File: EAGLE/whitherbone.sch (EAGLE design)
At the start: 227 parts, among them IC10 TXS0108ERGYR, IC11 TXS0108ERGYR, IC12 TPS2051BDGN, IC13 SN74AUC1G74, IC14 TPD4S012DRY, IC15 TPD4S012DRY, IC17 SN74LVC2G241DCUR, IC18 TL1963ADCQR, IC19 AP2112K-1.8TRG1 3.3V, IC2 SN74LVC1G07DCK, IC4 7805T, IC7 IP4283CZ10-TBR, IC8 IP4283CZ10-TBR, IC9 TDA19988BHN/C1,557, J1 1-1747981-1, Q2 32.768kHz, Q4 24 MHz, T1 BSS138W-7-F, T3 BSS138W-7-F, T4 BSS138W-7-F, U1 OSD3358-512M-BSM, U2 A3967SLBTR, X2 SCHA5B0200, X4 10118192-0001LF

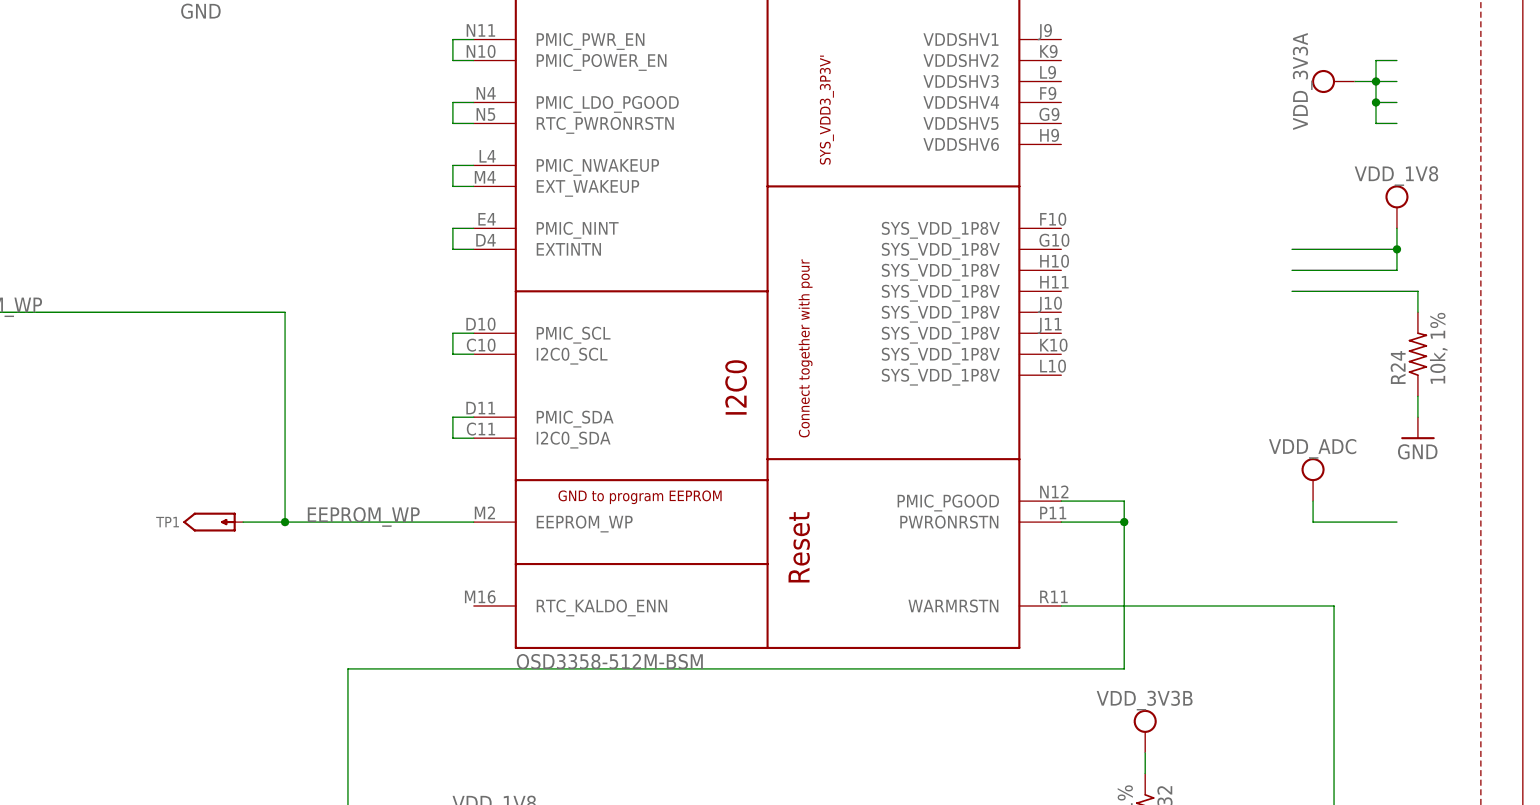
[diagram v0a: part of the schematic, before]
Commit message: Some minor power fixups
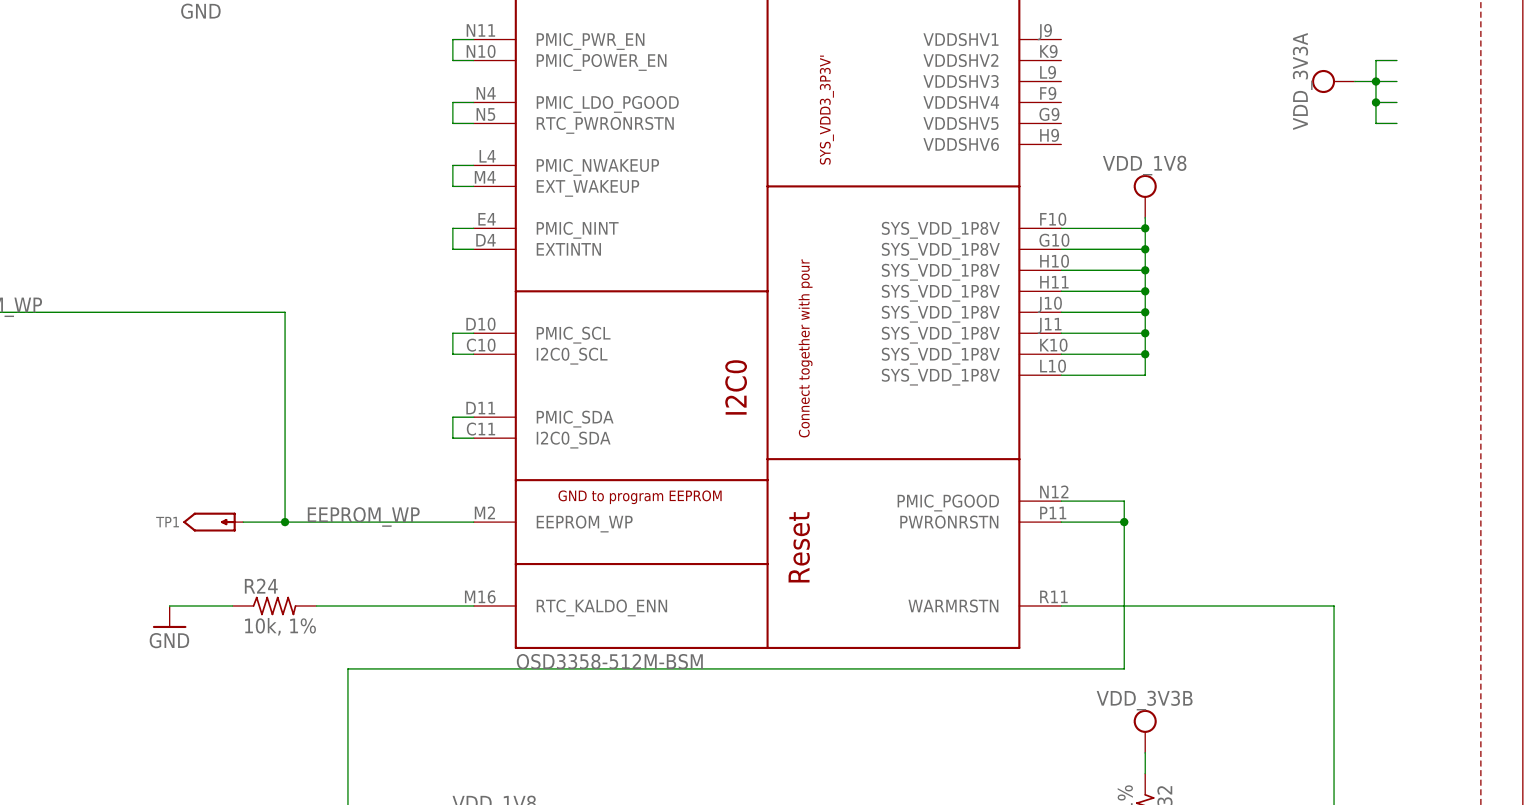
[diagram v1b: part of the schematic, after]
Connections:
- net N$22: now also U1A.RTC_KALDO_ENN
- net VDD_1V8: now also U1A.SYS_VDD_1P8V@1, U1A.SYS_VDD_1P8V@2, U1A.SYS_VDD_1P8V@3, U1A.SYS_VDD_1P8V@4, U1A.SYS_VDD_1P8V@5, U1A.SYS_VDD_1P8V@6, U1A.SYS_VDD_1P8V@7, U1A.SYS_VDD_1P8V@8
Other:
- moved on the sheet: R24
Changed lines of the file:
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@@
 <part name="SUPPLY7" library="GHI-PowerGoundSupply" deviceset="VDD_3V3A" device=""/>
 <part name="SUPPLY32" library="GHI-PowerGoundSupply" deviceset="VDD_5V" device=""/>
-<part name="SUPPLY4" library="GHI-PowerGoundSupply" deviceset="VDD_ADC" device=""/>
 <part name="SUPPLY11" library="GHI-PowerGoundSupply" deviceset="VDD_CORE" device=""/>
 <part name="SUPPLY5" library="GHI-PowerGoundSupply" deviceset="VDD_MPU" device=""/>
@@
 <instance part="SUPPLY14" gate="G$1" x="762" y="228.6"/>
 <instance part="SUPPLY6" gate="G$1" x="754.38" y="200.66" rot="R90"/>
-<instance part="SUPPLY12" gate="G$1" x="817.88" y="452.12"/>
+<instance part="SUPPLY12" gate="G$1" x="787.4" y="453.39"/>
 <instance part="SUPPLY7" gate="G$1" x="810.26" y="467.36" rot="R90"/>
 <instance part="SUPPLY32" gate="G$1" x="701.04" y="571.5"/>
-<instance part="SUPPLY4" gate="G$1" x="807.72" y="419.1"/>
 <instance part="SUPPLY11" gate="G$1" x="749.3" y="218.44"/>
 <instance part="SUPPLY5" gate="G$1" x="749.3" y="205.74" rot="R90"/>
@@
 <instance part="GND23" gate="1" x="673.1" y="477.52"/>
 <instance part="SUPPLY39" gate="G$1" x="789.94" y="548.64" rot="R270"/>
-<instance part="R24" gate="G$1" x="820.42" y="434.34" rot="R90"/>
-<instance part="GND10" gate="1" x="820.42" y="424.18"/>
+<instance part="R24" gate="G$1" x="681.99" y="403.86"/>
+<instance part="GND10" gate="1" x="669.29" y="401.32"/>
 <instance part="R8" gate="G$1" x="53.34" y="535.94" rot="R90"/>
 <instance part="R1" gate="G$1" x="459.74" y="154.94" rot="R90"/>
@@
 <pinref part="GND10" gate="1" pin="GND"/>
 <pinref part="R24" gate="G$1" pin="1"/>
-<wire x1="820.42" y1="426.72" x2="820.42" y2="429.26" width="0.1524" layer="91"/>
+<wire x1="669.29" y1="403.86" x2="676.91" y2="403.86" width="0.1524" layer="91"/>
 </segment>
 <segment>
@@
 <segment>
 <pinref part="SUPPLY12" gate="G$1" pin="VDD_1V8"/>
-<wire x1="817.88" y1="449.58" x2="817.88" y2="447.04" width="0.1524" layer="91"/>
-<wire x1="817.88" y1="447.04" x2="817.88" y2="444.5" width="0.1524" layer="91"/>
-<wire x1="817.88" y1="444.5" x2="805.18" y2="444.5" width="0.1524" layer="91"/>
-<wire x1="805.18" y1="447.04" x2="817.88" y2="447.04" width="0.1524" layer="91"/>
-<junction x="817.88" y="447.04"/>
+<wire x1="787.4" y1="450.85" x2="787.4" y2="449.58" width="0.1524" layer="91"/>
+<wire x1="787.4" y1="449.58" x2="787.4" y2="447.04" width="0.1524" layer="91"/>
+<wire x1="787.4" y1="447.04" x2="777.24" y2="447.04" width="0.1524" layer="91"/>
+<wire x1="777.24" y1="449.58" x2="787.4" y2="449.58" width="0.1524" layer="91"/>
+<junction x="787.4" y="449.58"/>
+<pinref part="U1" gate="A" pin="SYS_VDD_1P8V@3"/>
+<wire x1="777.24" y1="444.5" x2="787.4" y2="444.5" width="0.1524" layer="91"/>
+<wire x1="787.4" y1="444.5" x2="787.4" y2="447.04" width="0.1524" layer="91"/>
+<pinref part="U1" gate="A" pin="SYS_VDD_1P8V@4"/>
+<wire x1="777.24" y1="441.96" x2="787.4" y2="441.96" width="0.1524" layer="91"/>
+<wire x1="787.4" y1="441.96" x2="787.4" y2="444.5" width="0.1524" layer="91"/>
+<pinref part="U1" gate="A" pin="SYS_VDD_1P8V@5"/>
+<wire x1="777.24" y1="439.42" x2="787.4" y2="439.42" width="0.1524" layer="91"/>
+<wire x1="787.4" y1="439.42" x2="787.4" y2="441.96" width="0.1524" layer="91"/>
+<wire x1="777.24" y1="436.88" x2="787.4" y2="436.88" width="0.1524" layer="91"/>
+<wire x1="787.4" y1="436.88" x2="787.4" y2="439.42" width="0.1524" layer="91"/>
+<pinref part="U1" gate="A" pin="SYS_VDD_1P8V@7"/>
+<wire x1="777.24" y1="434.34" x2="787.4" y2="434.34" width="0.1524" layer="91"/>
+<wire x1="787.4" y1="434.34" x2="787.4" y2="436.88" width="0.1524" layer="91"/>
+<pinref part="U1" gate="A" pin="SYS_VDD_1P8V@8"/>
+<wire x1="777.24" y1="431.8" x2="787.4" y2="431.8" width="0.1524" layer="91"/>
+<wire x1="787.4" y1="431.8" x2="787.4" y2="434.34" width="0.1524" layer="91"/>
+<junction x="787.4" y="447.04"/>
+<junction x="787.4" y="444.5"/>
+<junction x="787.4" y="441.96"/>
+<junction x="787.4" y="439.42"/>
+<junction x="787.4" y="436.88"/>
+<junction x="787.4" y="434.34"/>
+<pinref part="U1" gate="A" pin="SYS_VDD_1P8V@1"/>
+<pinref part="U1" gate="A" pin="SYS_VDD_1P8V@2"/>
+<pinref part="U1" gate="A" pin="SYS_VDD_1P8V@6"/>
 </segment>
 <segment>
@@
 <net name="VDD_ADC" class="0">
 <segment>
-<pinref part="SUPPLY4" gate="G$1" pin="VDD_ADC"/>
-<wire x1="817.88" y1="414.02" x2="807.72" y2="414.02" width="0.1524" layer="91"/>
-<wire x1="807.72" y1="414.02" x2="807.72" y2="416.56" width="0.1524" layer="91"/>
-</segment>
-<segment>
 <pinref part="SUPPLY19" gate="G$1" pin="VDD_ADC"/>
 <wire x1="327.66" y1="546.1" x2="312.42" y2="546.1" width="0.1524" layer="91"/>
@@
 <net name="N$22" class="0">
 <segment>
-<wire x1="805.18" y1="441.96" x2="820.42" y2="441.96" width="0.1524" layer="91"/>
+<wire x1="706.12" y1="403.86" x2="687.07" y2="403.86" width="0.1524" layer="91"/>
 <pinref part="R24" gate="G$1" pin="2"/>
-<wire x1="820.42" y1="441.96" x2="820.42" y2="439.42" width="0.1524" layer="91"/>
+<pinref part="U1" gate="A" pin="RTC_KALDO_ENN"/>
 </segment>
 </net>

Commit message: Move WiFi signals to 1.8V and remove level shifters
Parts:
- removed C10: 1uF, rcl:C-USC0402K
- removed C19: 10uF, 6.3V, rcl:C-USC0603K
- removed C25, C45: .1uF, 6.3V, rcl:C-USC0402K
- removed D2: STPS140A DNP, GHI:DIODE_SMA
- removed D3, D4: STPS140A, GHI:DIODE_SMA
- removed D8: BAT54C, diode:BAT54C
- removed IC10, IC11: TXS0108ERGYR, GHI-IC:TXS0108ERGYR
- removed IC18: TL1963ADCQR, GHI-IC:TL1963A
- removed IC19: AP2112K-1.8TRG1 3.3V, GHI:5PIN_REG
- removed R10, R11: 150k, rcl:R-US_R0402
- removed R106: 1.5k, rcl:R-US_R0402
- removed R108, R109, R97: DNP 1k, rcl:R-US_R0402
- removed R126, R127, R128, R129, R130, R131, R134, R135, R136, R86: 33, 5%, rcl:R-US_R0603
- removed R89: 1k, rcl:R-US_R0402
- removed R91: 0 DNP, rcl:R-US_R0402
- removed R93: 7.15k, rcl:R-US_R0402
- removed R94: 4.12k, rcl:R-US_R0402
- removed R95: 1M, rcl:R-US_R0402
- removed TP23: PTR1B1,27, testpad:PTR1B1,27
- added FB7: 1k BLM15AG102SN1D, rcl:R-US_R0402
- FB1: value 220 Ohm 800mA -> 1k BLM15AG102SN1D; device GHI-BasicComponents:FB-(INCH)-0805 -> rcl:R-US_R0402
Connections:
- removed net 5V_IN: C19.1, D8.CC, FB1.P$2, IC18.IN, R95.1
- removed net ALT.BT.EN: IC11.B3, R135.2
- removed net ALT.BUFF.OE: IC10.OE, IC11.OE, R106.1, R131.1
- removed net ALT.WL.CLK: IC10.B5, R126.2
- removed net ALT.WL.CMD: IC10.B6, R86.2
- removed net ALT.WL.D0: IC10.B1, R130.2
- removed net ALT.WL.D1: IC10.B2, R129.2
- removed net ALT.WL.D2: IC10.B3, R128.2
- removed net ALT.WL.D3: IC10.B4, R127.2
- removed net ALT.WL.EN: IC11.B2, R136.2
- removed net ALT.WL.IRQ: IC11.B8, R134.2
- removed net BT_EN.SIP: R135.1, U1D.MII1_TXD0
- removed net BT_HCI_CTS.SIP: IC11.B5, R108.1, U1D.MDIO
- removed net BT_HCI_RTS.SIP: IC11.B7, R109.1, U1D.MDC
- removed net BT_HCI_RX.SIP: IC11.B6, U1D.MII1_RXD3
- removed net BT_HCI_TX.SIP: IC11.B1, U1D.MII1_RXD2
- removed net CLKOUT2: IC11.B4
- removed net LS_BUF_OE: R131.2, U1D.MII1_RX_CLK
- removed net N$30: R9.2
- removed net N$9: IC18.ADJ, R93.2, R94.1
- removed net SELECT_5V: D2.K, D3.K, D4.K, FB1.P$1, R97.1, TP23.TP
- removed net SLOW_CLK: IC11.A4, R91.1
- removed net WL_EN.SIP: R136.1, U1D.MII1_TX_CLK
- removed net WL_IRQ.SIP: R134.1, U1D.MII1_TXD1
- removed net WL_SDIO_CLK.SIP: R126.1, U1D.MII1_RXD1
- removed net WL_SDIO_CMD.SIP: R86.1, U1D.MII1_TX_EN
- removed net WL_SDIO_D0.SIP: R130.1, U1D.MII1_RX_DV
- removed net WL_SDIO_D1.SIP: R129.1, U1D.MII1_TXD3
- removed net WL_SDIO_D2.SIP: R128.1, U1D.MII1_TXD2
- removed net WL_SDIO_D3.SIP: R127.1, U1D.MII1_COL
- new net VDD_3V3A: U1A.SYS_VDD3_3P3V@4, U1A.SYS_VDD3_3P3V@5, U1A.SYS_VDD3_3P3V@6, U1A.SYS_VDD3_3P3V@7, U1A.SYS_VDD3_3P3V@8, U1A.VDDSHV1, U1A.VDDSHV2, U1A.VDDSHV3, U1A.VDDSHV4, U1A.VDDSHV6
- net 1.8V-WIFI: now also FB7.1; no longer C25.1, IC10.VCCA, IC11.VCCA, IC19.VOUT
- net 3.3V-WIFI: now also FB1.1, R9.2; no longer C10.1, C45.1, IC10.VCCB, IC11.VCCB, IC18.OUT, IC19.EN, IC19.VIN, R93.1
- net 32.768KHZ: no longer R91.2
- net BT_EN: now also U1D.MII1_TXD0; no longer IC11.A3, R11.1
- net BT_HCI_CTS: now also U1D.MDIO; no longer IC11.A7
- net BT_HCI_RTS: now also U1D.MDC; no longer IC11.A5
- net BT_HCI_RX: now also U1D.MII1_RXD3; no longer IC11.A1
- net BT_HCI_TX: now also U1D.MII1_RXD2; no longer IC11.A6
- net GND: no longer C10.2, C19.2, C25.2, C45.2, D8.A2, IC10.GND, IC10.TP, IC11.GND, IC11.TP, IC18.GND1, IC18.GND2, IC19.GND, R10.2, R106.2, R108.2, R109.2, R11.2, R94.2, R95.2
- net N$5: now also U1B.AIN7, U1B.PMIC_MUX_OUT; no longer IC18.SHDN#, R89.2, R97.2
- net SYS_5V: no longer D2.A
- net USB_DC: no longer D4.A
- net VDD_1V8: now also FB7.2, U1A.VDDSHV5
- net VDD_3V3B: now also FB1.2; no longer R89.1
- net VDD_5V: no longer D3.A
- net WL_EN: now also U1D.MII1_TX_CLK; no longer IC11.A2, R10.1
- net WL_IRQ: now also U1D.MII1_TXD1; no longer IC11.A8
- net WL_SDIO_CLK: now also U1D.MII1_RXD1; no longer IC10.A5
- net WL_SDIO_CMD: now also U1D.MII1_TX_EN; no longer IC10.A6
- net WL_SDIO_D0: now also U1D.MII1_RX_DV; no longer IC10.A1
- net WL_SDIO_D1: now also U1D.MII1_TXD3; no longer IC10.A2
- net WL_SDIO_D2: now also U1D.MII1_TXD2; no longer IC10.A3
- net WL_SDIO_D3: now also U1D.MII1_COL; no longer IC10.A4
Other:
- note added: "These signals are all 1.8V"
- note removed: "1.8V WiFi Power Regulator"

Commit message: Copied BigEasyDriver
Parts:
- removed U2: A3967SLBTR, A3967SLBTR:A3967SLBTR
- added C10, C13, C14, C15, C18: .1uf, SparkFun:CAP0402-CAP
- added C17: .22uF, SparkFun:CAP0402-CAP
- added FB8: 1k BLM15AG102SN1D, rcl:R-US_R0402
- added IC1: A4983, SparkFun:A4983
- added JP3: (no value), SparkFun:M04PTH
- added JP5: (no value), BigEasyDriver_v11:M04SCREW_LOCK
- added R10, R18: .11, SparkFun:RESISTOR2010
- added R11, R14, R15, R20, R21, R22, R23: 20K, SparkFun:RESISTOR0402-RES
- added R16: 10K, SparkFun:TRIMPOTSMD
- added R25: 2.49K, SparkFun:RESISTOR0402-RES
- added TP2: TPPAD1-13, testpad:TPPAD1-13
- R12: value 10K -> 20K; device Seeed-Resistor:DIP-VR-TOP-ADJ-10K(3P-9.5X9.5X5MM) -> SparkFun:RESISTOR0402-RES
- R13: value 2K -> 20K; device Seeed-Resistor:SMD-RES-2K-1%-1/10W(0603) -> SparkFun:RESISTOR0402-RES
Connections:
- new net COILA+: IC1.OUT1B, JP3.4, JP5.4
- new net COILA-: IC1.OUT1A, JP3.3, JP5.3
- new net COILB+: IC1.OUT2B, JP3.1, JP5.1
- new net COILB-: IC1.OUT2A, JP3.2, JP5.2
- new net CUR_REF: IC1.REF, R16.WIPER, TP2.TP
- new net DIR: IC1.DIR, R22.1
- new net ENABLE: IC1.ENABLE, R21.1
- new net MS1: IC1.MS1, R11.1
- new net MS2: IC1.MS2, R12.1
- new net MS3: IC1.MS3, R13.1
- new net MVCC: C13.1, IC1.VDD, R11.2, R12.2, R13.2, R14.2, R15.2, R22.2, R23.2, R25.1
- new net N$30: IC1.ROSC, R20.1
- new net N$32: IC1.SENSE1, R10.2
- new net N$46: C17.1, IC1.VREG
- new net N$47: C18.1, IC1.VCP
- new net N$48: R16.CCW, R25.2
- new net N$9: C10.1, IC1.CP1
- new net RESET: IC1.RESET, R15.1
- new net SLEEP: IC1.SLEEP, R14.1
- new net STEP: IC1.STEP, R23.1
- net 12VDC: now also C14.1, C15.1, C18.2, IC1.VBB1, IC1.VBB2
- net GND: now also C13.2, C14.2, C15.2, C17.2, IC1.GND@1, IC1.GND@2, IC1.GND_PAD, R10.1, R16.CW, R18.1, R20.2, R21.2; no longer R13.1
- net N$10: now also C10.2, IC1.CP2; no longer R12.3, U2.REF
- net N$31: now also IC1.SENSE2, R18.2; no longer R12.1, R13.2
- net VDD_5V: no longer R12.2, U2.VCC
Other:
- note added: "Attribution 3.0 US License"
- note added: "BigEasyDriver v1.2 by Brian Schmalz is"
- note added: "Current adj pot"
- note added: "Motor current 0mA to over 2A/phase"
- note added: "licensed under a Creative Commons"
- note added: "www.schmalzhaus.com/BigEasyDriver"
- note removed: "Motor Driver"
